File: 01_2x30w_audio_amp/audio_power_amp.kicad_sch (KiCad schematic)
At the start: 51 parts, among them U801 TPA3118D2

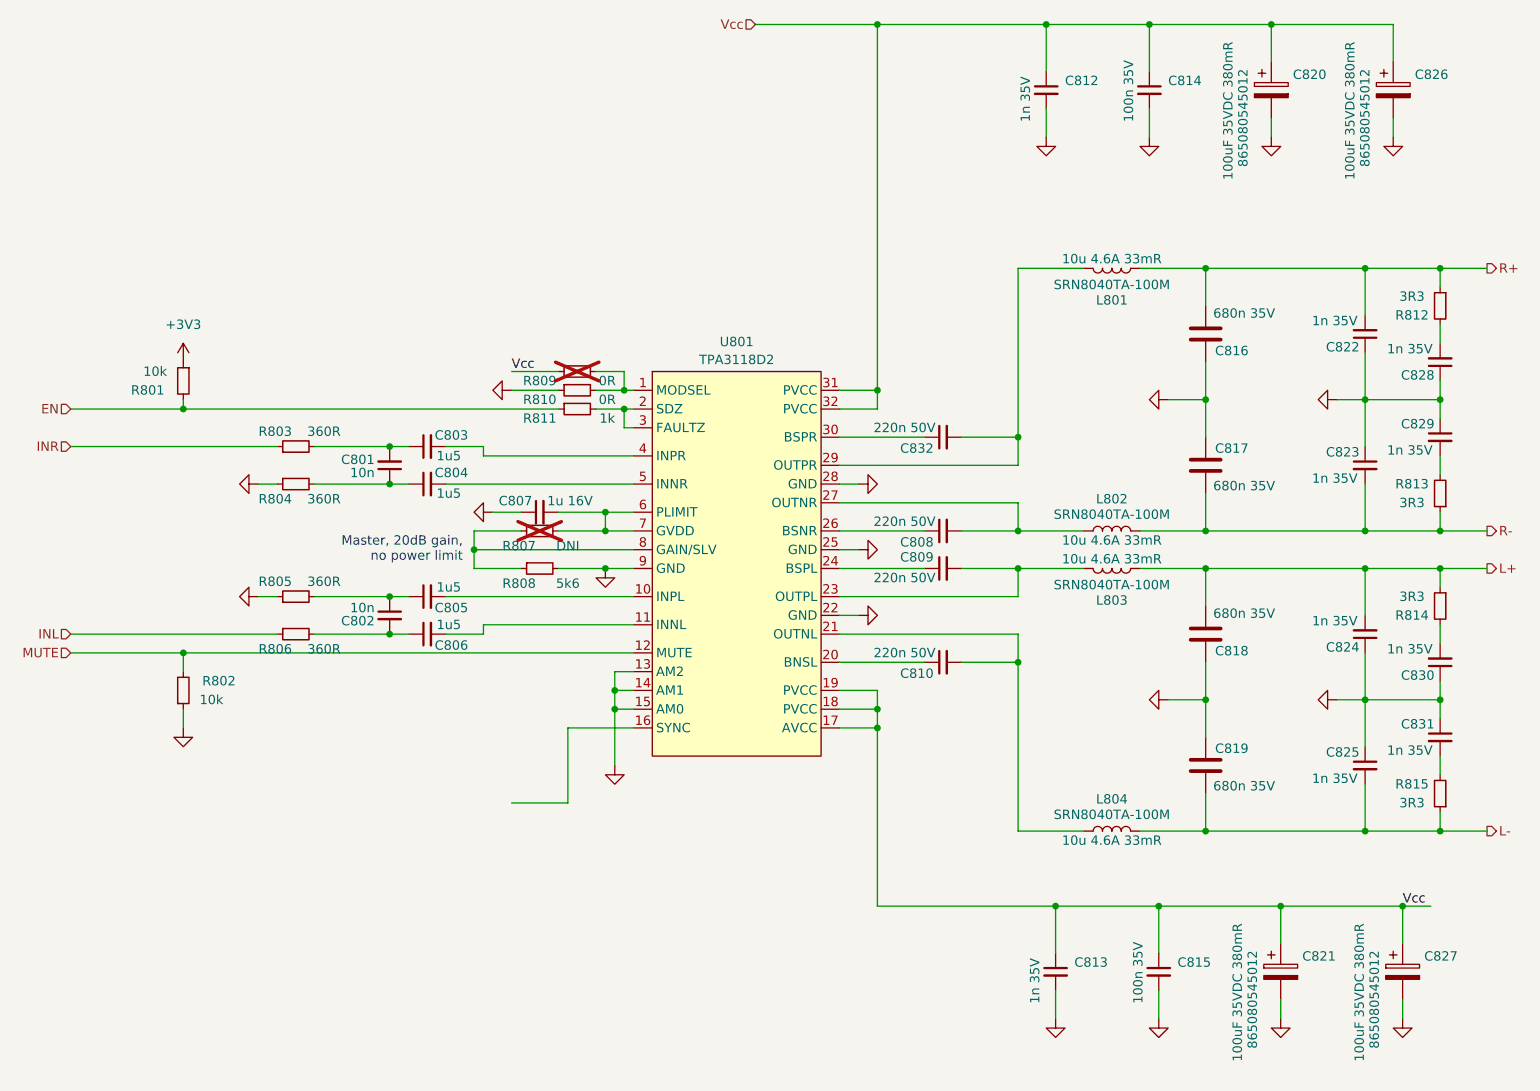
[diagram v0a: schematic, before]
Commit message: Module no. 1 completely redesigned
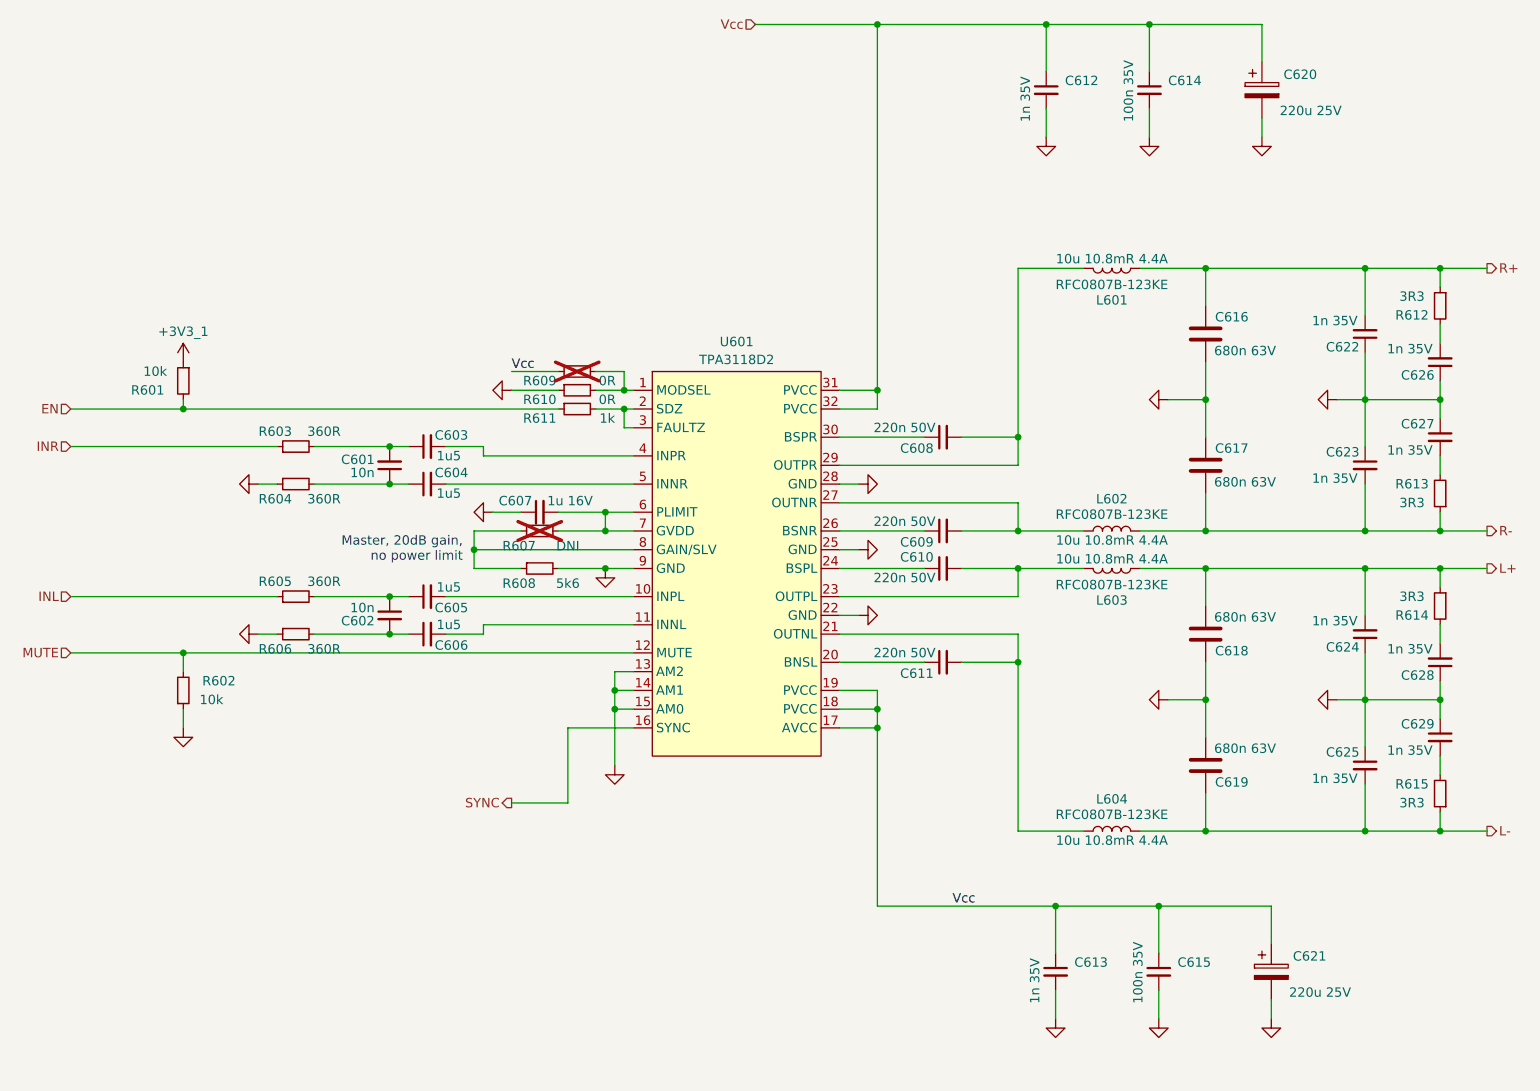
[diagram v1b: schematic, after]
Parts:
- removed C817, C818, C819: 680n 35V, Capacitor_SMD:C_1206_3216Metric, symbol Device:C
- removed C820, C821, C826, C827: 865080545012, Capacitor_SMD:C_Elec_6.3x7.7, symbol Device:C_Polarized
- removed L802, L803, L804: SRN8040TA-100M, Inductor_SMD:L_Bourns_SRN8040TA, symbol Device:L
- added C616, C618, C619: B32529C684J, Capacitor_THT:C_Rect_L7.2mm_W2.5mm_P5.00mm_FKS2_FKP2_MKS2_MKP2, symbol Device:C
- added C620, C621: A750KS227M1EAAE015, Capacitor_THT:CP_Radial_D8.0mm_P3.50mm, symbol Device:C_Polarized
- added L602, L603, L604: RFC0807B-123KE, libs:SER1360182KLD, symbol Device:L
- C617: renamed from C816; value 680n 35V -> B32529C684J; footprint Capacitor_SMD:C_1206_3216Metric -> Capacitor_THT:C_Rect_L7.2mm_W2.5mm_P5.00mm_FKS2_FKP2_MKS2_MKP2
- L601: renamed from L801; value SRN8040TA-100M -> RFC0807B-123KE; footprint Inductor_SMD:L_Bourns_SRN8040TA -> libs:SER1360182KLD
- renumbered C801 to C601, C802 to C602, C803 to C603, C804 to C604, C805 to C605, C806 to C606, C807 to C607, C808 to C608, C832 to C609, C809 to C610, C810 to C611, C812 to C612, C813 to C613, C814 to C614, C815 to C615, C823 to C622, C822 to C623, C824 to C624, C825 to C625, C829 to C626, C828 to C627, C830 to C628, C831 to C629, R801 to R601, R802 to R602, R803 to R603, R804 to R604, R805 to R605, R806 to R606, R807 to R607, R808 to R608, R809 to R609, R810 to R610, R811 to R611, R813 to R612, R812 to R613, R814 to R614, R815 to R615, U801 to U601
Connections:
- net GND: now also R606.1, C616.1, C618.2, C619.1, C620.2, C621.2; no longer R605.1
- net INL: now also R605.1; no longer R606.1
- net L+: now also C618.1, L603.1
- net L-: now also C619.2, L604.1
- net R+: now also C622.2, R612.1, C616.2; no longer C617.1, C623.2, R613.1
- net R-: now also C617.1, C623.2, R613.1, L602.2; no longer C622.2, R612.1
- net Vcc: now also C620.1, C621.1
- net at L601.1, U601.29 (OUTPR): now also C608.2; no longer C609.2
- net at U601.27 (OUTNR): now also C609.2, L602.1; no longer C608.2
- net at C610.2, U601.23 (OUTPL): now also L603.2
- net at C611.2, U601.21 (OUTNL): now also L604.2
- net SYNC: now reaches U601.16 (SYNC)
- net at U601.26 (BSNR): now also C609.1; no longer C608.1
- net at U601.30 (BSPR): now also C608.1; no longer C609.1
- net +3V3 renamed +3V3_1
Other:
- moved on the sheet: C608, C609, C617, C622, C623, C626, C627, R612, R613
